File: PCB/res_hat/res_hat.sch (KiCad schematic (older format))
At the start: 55 parts, among them IC1 MCP4725A0T-E_CH, IC2 MCP4725A0T-E_CH, IC3 UCC27324D, J1 Conn_02x20_Odd_Even, J10 Conn_01x02, J11 Jack-DC, J2 Conn_02x04_Odd_Even, J3 Conn_01x03, J4 Conn_01x06, J5 Conn_Coaxial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

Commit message: add hexa i2c adress
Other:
- note added: "I2C adres (bin): 1000101\nI2C adres (hex): 0x45"
- note added: "I2C adres (bin): 1000110\nI2C adres (hex): 0x46"
- note added: "I2C adres (bin): 1100000\nI2C adres (hex): 0x60"
- note added: "I2C adres (bin): 1100001\nI2C adres (hex): 0x61"
- note removed: "I2C adres : 1000101"
- note removed: "I2C adres : 1000110"
- note removed: "I2C adres : 1100000"
- note removed: "I2C adres : 1100001"
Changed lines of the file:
@@
 $EndComp
 Text Notes 9900 4500 0    50   ~ 0
-I2C adres : 1000110
+I2C adres (bin): 1000110\nI2C adres (hex): 0x46
 Connection ~ 9650 4100
 Wire Wire Line
@@
 $EndComp
 Text Notes 9800 2300 0    50   ~ 0
-I2C adres : 1000101
+I2C adres (bin): 1000101\nI2C adres (hex): 0x45
 Text Label 9500 2200 0    50   ~ 0
 SDA
@@
 Connection ~ 5650 3000
 Text Notes 4650 3850 0    50   ~ 0
-I2C adres : 1100001
+I2C adres (bin): 1100001\nI2C adres (hex): 0x61
 Text Notes 4550 1550 0    50   ~ 0
-I2C adres : 1100000
+I2C adres (bin): 1100000\nI2C adres (hex): 0x60
 $Comp
 L power:GND #PWR0144

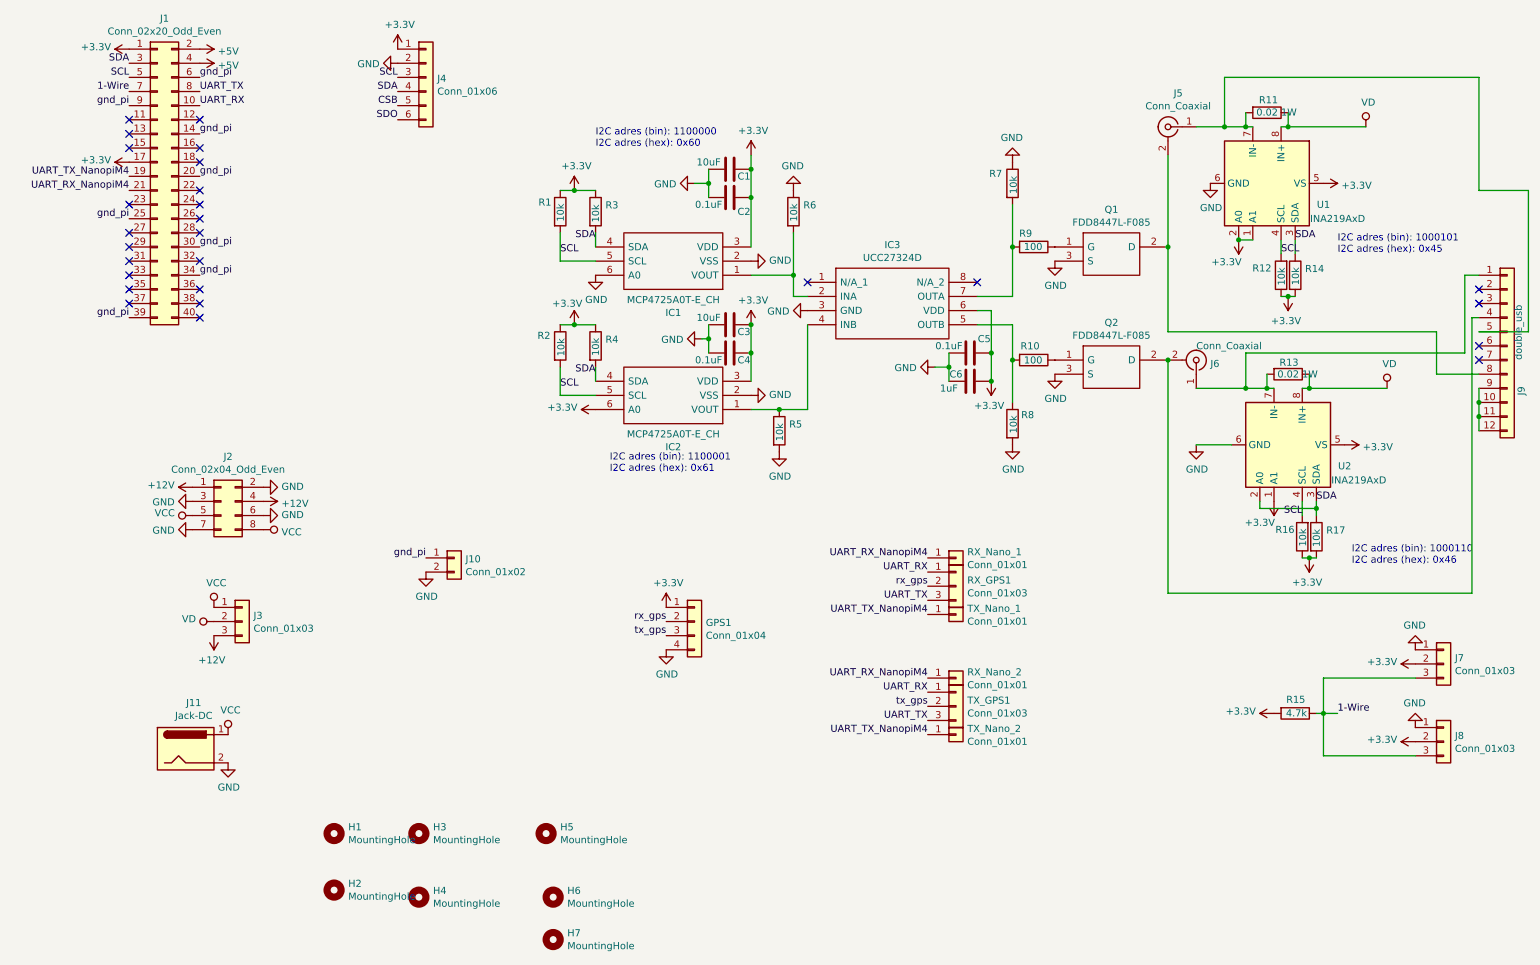
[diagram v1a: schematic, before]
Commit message: change DC for XT30, change controle res for pwm
add ds1050Z-025+ change for xt30 connector for in alim
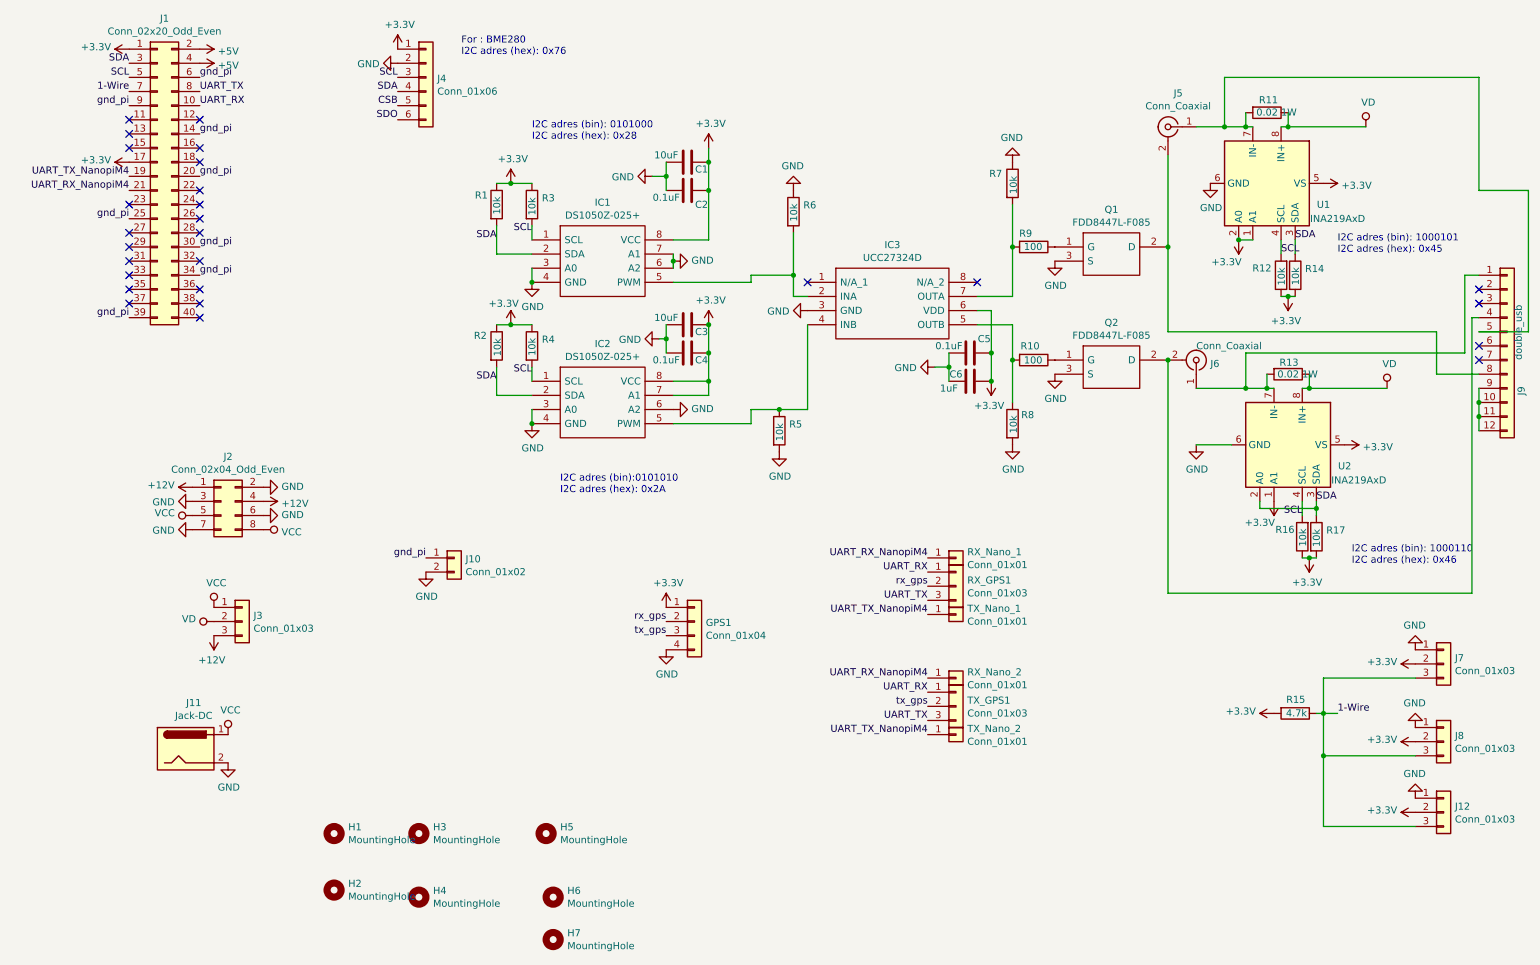
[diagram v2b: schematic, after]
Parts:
- removed IC1, IC2: MCP4725A0T-E_CH, mcp4725:SOT95P270X145-6N, symbol MCP4725A0T-E_CH:MCP4725A0T-E_CH
- added IC1, IC2: DS1050Z-025+, DS1050Z:SOIC127P600X175-8N, symbol DS1050Z-010+:DS1050Z-010+
- added J12: Conn_01x03, Connector_Molex:Molex_KK-254_AE-6410-03A_1x03_P2.54mm_Vertical, symbol Connector_Generic:Conn_01x03
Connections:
- net +3V3: now also IC1.8 (VCC), IC2.7 (A1), IC2.8 (VCC), J12.2 (Pin_2)
- net 1-Wire: now also J12.3 (Pin_3)
- net GND: now also IC1.3 (A0), IC1.4 (GND), IC1.6 (A2), IC1.7 (A1), IC2.3 (A0), IC2.4 (GND), IC2.6 (A2), J12.1 (Pin_1)
- net SCL: now also R3.2, R4.2, IC1.1 (SCL), IC2.1 (SCL); no longer R1.2, R2.2
- net SDA: now also R1.2, R2.2, IC1.2 (SDA), IC2.2 (SDA); no longer R3.2, R4.2
- net at IC3.2 (INA), R6.2: now also IC1.5 (PWM)
- net at IC3.4 (INB), R5.1: now also IC2.5 (PWM)
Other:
- note added: "For : BME280 \nI2C adres (hex): 0x76"
- note added: "I2C adres (bin): 0101000\nI2C adres (hex): 0x28"
- note added: "I2C adres (bin):0101010\nI2C adres (hex): 0x2A"
- note removed: "I2C adres (bin): 1100000\nI2C adres (hex): 0x60"
- note removed: "I2C adres (bin): 1100001\nI2C adres (hex): 0x61"
- moved on the sheet: C1, C2, C3, C4, R1, R2, R3, R4

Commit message: ajust all board
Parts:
- Q1, Q2: LCSC C99591 -> C99591 or C154314
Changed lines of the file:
@@
 Sheet 1 1
 Title "rpi_hat_alim_resist"
-Date "2020-02-29"
-Rev "1.0"
+Date "2020-10-30"
+Rev "3.0"
 Comp ""
 Comment1 ""
@@
 F 8 "ON Semiconductor" H 8450 1750 50  0001 L CNN "Manufacturer_Name"
 F 9 "FDD8447L-F085" H 8450 1650 50  0001 L CNN "Manufacturer_Part_Number"
-F 10 "C99591" H 7800 2250 50  0001 C CNN "LCSC"
+F 10 "C99591 or C154314 " H 7800 2250 50  0001 C CNN "LCSC"
 	1    7800 2250
 	1    0    0    -1
@@
 F 8 "ON Semiconductor" H 8450 2550 50  0001 L CNN "Manufacturer_Name"
 F 9 "FDD8447L-F085" H 8450 2450 50  0001 L CNN "Manufacturer_Part_Number"
-F 10 "C99591" H 7800 3050 50  0001 C CNN "LCSC"
+F 10 "C99591 or C154314 " H 7800 3050 50  0001 C CNN "LCSC"
 	1    7800 3050
 	1    0    0    -1

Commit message: ajust terminal position in relay board
change hole diameter in res_board
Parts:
- H1, H2, H3, H4, H5, H6, H7: footprint MountingHole:MountingHole_2.7mm_M2.5 -> MountingHole:MountingHole_3.2mm_M3
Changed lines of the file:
@@
 F 0 "H1" H 2800 6446 50  0000 L CNN
 F 1 "MountingHole" H 2800 6355 50  0000 L CNN
-F 2 "MountingHole:MountingHole_2.7mm_M2.5" H 2700 6400 50  0001 C CNN
+F 2 "MountingHole:MountingHole_3.2mm_M3" H 2700 6400 50  0001 C CNN
 F 3 "~" H 2700 6400 50  0001 C CNN
 	1    2700 6400
@@
 F 0 "H3" H 3400 6446 50  0000 L CNN
 F 1 "MountingHole" H 3400 6355 50  0000 L CNN
-F 2 "MountingHole:MountingHole_2.7mm_M2.5" H 3300 6400 50  0001 C CNN
+F 2 "MountingHole:MountingHole_3.2mm_M3" H 3300 6400 50  0001 C CNN
 F 3 "~" H 3300 6400 50  0001 C CNN
 	1    3300 6400
@@
 F 0 "H2" H 2800 6846 50  0000 L CNN
 F 1 "MountingHole" H 2800 6755 50  0000 L CNN
-F 2 "MountingHole:MountingHole_2.7mm_M2.5" H 2700 6800 50  0001 C CNN
+F 2 "MountingHole:MountingHole_3.2mm_M3" H 2700 6800 50  0001 C CNN
 F 3 "~" H 2700 6800 50  0001 C CNN
 	1    2700 6800
@@
 F 0 "H4" H 3400 6896 50  0000 L CNN
 F 1 "MountingHole" H 3400 6805 50  0000 L CNN
-F 2 "MountingHole:MountingHole_2.7mm_M2.5" H 3300 6850 50  0001 C CNN
+F 2 "MountingHole:MountingHole_3.2mm_M3" H 3300 6850 50  0001 C CNN
 F 3 "~" H 3300 6850 50  0001 C CNN
 	1    3300 6850
@@
 F 0 "H5" H 4300 6446 50  0000 L CNN
 F 1 "MountingHole" H 4300 6355 50  0000 L CNN
-F 2 "MountingHole:MountingHole_2.7mm_M2.5" H 4200 6400 50  0001 C CNN
+F 2 "MountingHole:MountingHole_3.2mm_M3" H 4200 6400 50  0001 C CNN
 F 3 "~" H 4200 6400 50  0001 C CNN
 	1    4200 6400
@@
 F 0 "H6" H 4350 6896 50  0000 L CNN
 F 1 "MountingHole" H 4350 6805 50  0000 L CNN
-F 2 "MountingHole:MountingHole_2.7mm_M2.5" H 4250 6850 50  0001 C CNN
+F 2 "MountingHole:MountingHole_3.2mm_M3" H 4250 6850 50  0001 C CNN
 F 3 "~" H 4250 6850 50  0001 C CNN
 	1    4250 6850
@@
 F 0 "H7" H 4350 7196 50  0000 L CNN
 F 1 "MountingHole" H 4350 7105 50  0000 L CNN
-F 2 "MountingHole:MountingHole_2.7mm_M2.5" H 4250 7150 50  0001 C CNN
+F 2 "MountingHole:MountingHole_3.2mm_M3" H 4250 7150 50  0001 C CNN
 F 3 "~" H 4250 7150 50  0001 C CNN
 	1    4250 7150
